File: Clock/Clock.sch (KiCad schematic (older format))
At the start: 39 parts, among them J1 Conn_01x16, J2 Conn_01x16, SW1 SW_Push, SW2 SW_Push, SW3 SW_Push, SW4 SW_Push, U1 74LS76, U2 74LS76, U3 74LS08, U4 74LS08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

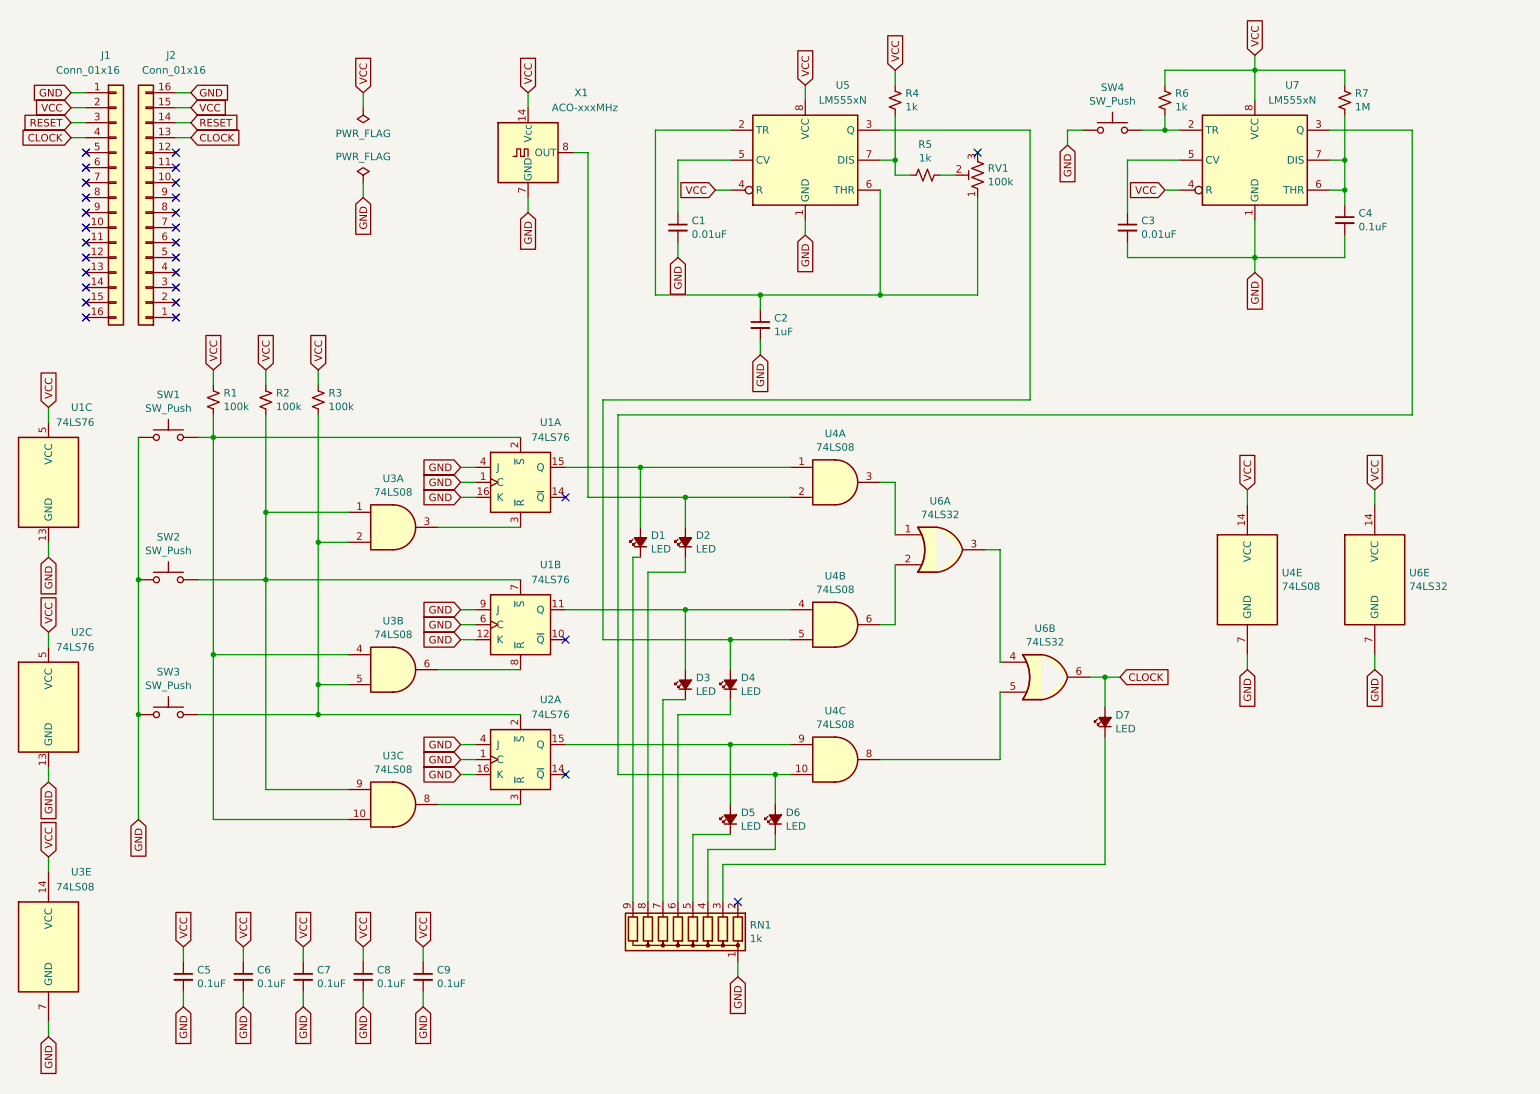
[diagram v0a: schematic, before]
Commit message: Fixed floating inputs; improved power; added parts list; replaced JK latches
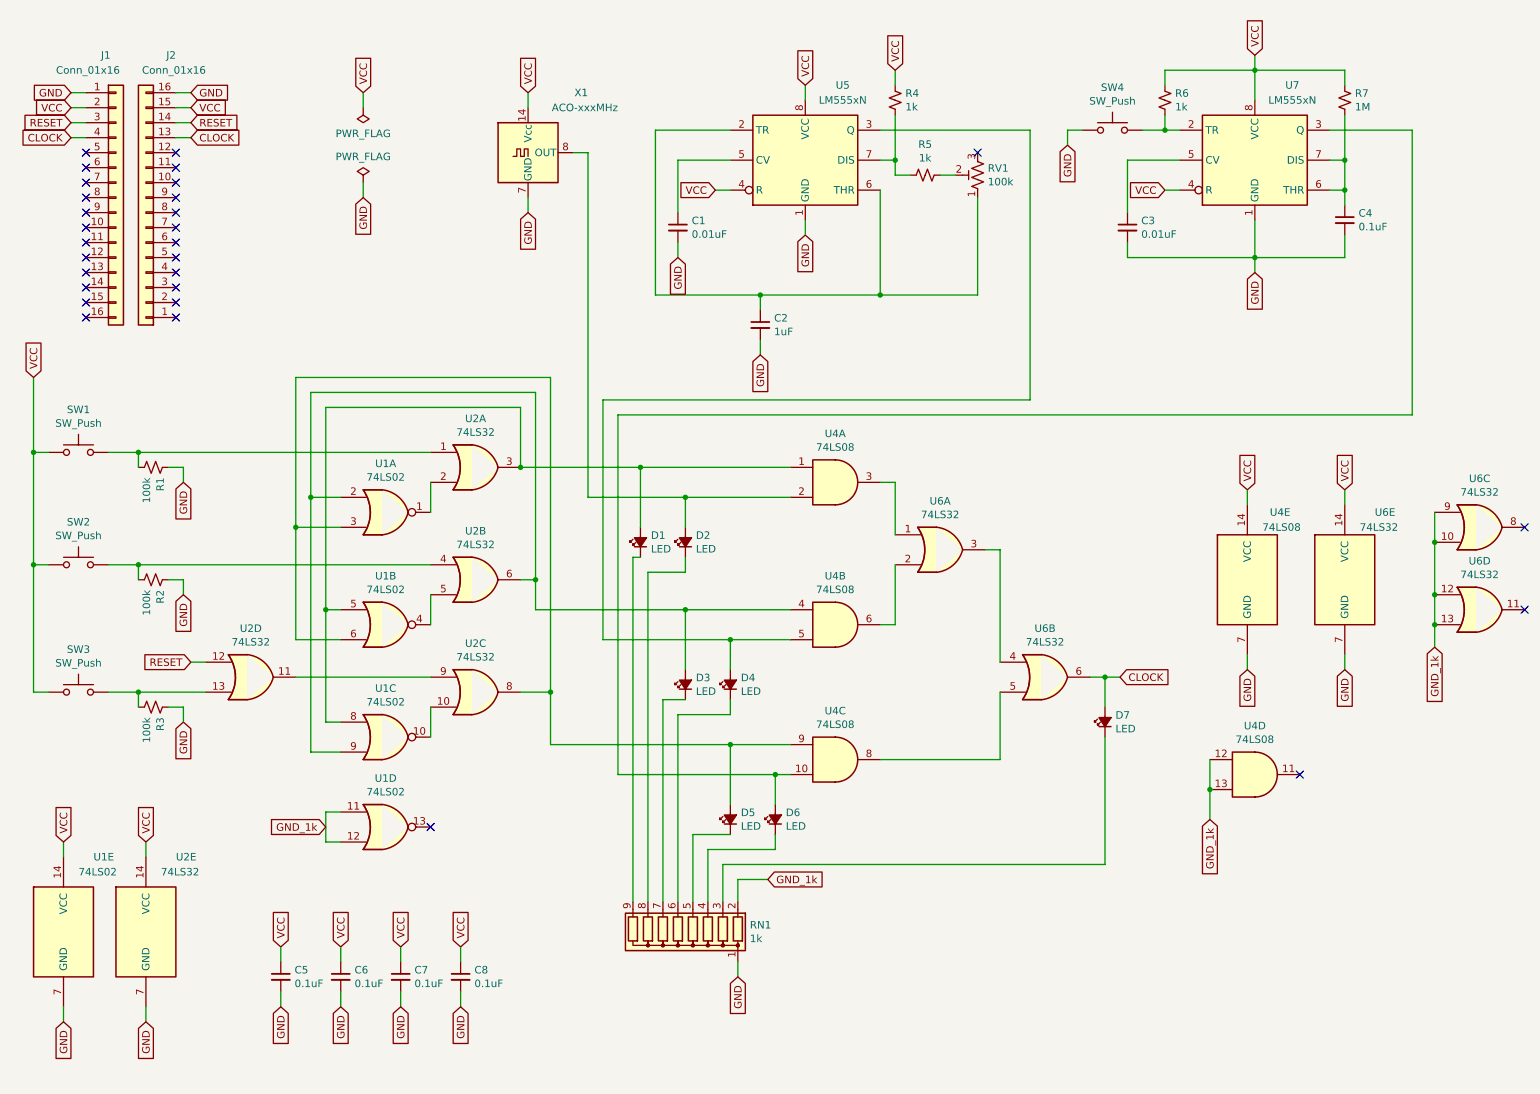
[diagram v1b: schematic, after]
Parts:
- removed C9: 0.1uF, Capacitor_THT:C_Disc_D4.3mm_W1.9mm_P5.00mm, symbol Device:C_Small
- removed U1, U2: 74LS76, Package_DIP:DIP-16_W7.62mm, symbol 74xx:74LS76
- removed U3: 74LS08, Package_DIP:DIP-14_W7.62mm, symbol 74xx:74LS08
- added U1: 74LS02, Package_DIP:DIP-14_W7.62mm, symbol 74xx:74LS02
- added U2: 74LS32, Package_DIP:DIP-14_W7.62mm, symbol 74xx:74LS32
- added unit 4 of U4
- added unit 3 of U6
- added unit 4 of U6
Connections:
- net GND: now also R1.1, R2.1, R3.1, U1.7 (GND), U2.7 (GND); no longer SW1.1, SW2.1, SW3.1
- net RESET: now also U2.12
- net VCC: now also SW1.1, SW2.1, SW3.1, U1.14 (VCC), U2.14 (VCC); no longer R1.1, R2.1, R3.1
- net at D1.2 (A), U4.1: now also U1.5, U1.8, U2.3
- net at R1.2, SW1.2: now also U2.1
- net at D3.2 (A), U4.4: now also U1.2, U1.9, U2.6
- net at R2.2, SW2.2: now also U2.4
- net at D5.2 (A), U4.9: now also U1.3, U1.6, U2.8
- net at R3.2, SW3.2: now also U2.13
- net GND_1k: now reaches RN1.2 (R1)
- net GND_1k: now also U1.11, U1.12, U4.12, U4.13, U6.10, U6.12, U6.13, U6.9
- new net: U1.1, U2.2
- new net: U1.4, U2.5
- new net: U1.10, U2.10
- new net: U2.11, U2.9
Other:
- moved on the sheet: C5, C6, C7, C8, U6E

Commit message: Update all boards to r3, and update revision log and gitignore
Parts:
- RV1: value 100k -> 1M; footprint Potentiometer_THT:Potentiometer_Alps_RK09Y11_Single_Horizontal -> Potentiometer_THT:Potentiometer_Bourns_PTV09A-1_Single_Vertical
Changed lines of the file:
@@
 P 7100 1600
 F 0 "RV1" H 7032 1554 50  0000 R CNN
-F 1 "100k" H 7032 1645 50  0000 R CNN
-F 2 "Potentiometer_THT:Potentiometer_Alps_RK09Y11_Single_Horizontal" H 7100 1600 50  0001 C CNN
+F 1 "1M" H 7032 1645 50  0000 R CNN
+F 2 "Potentiometer_THT:Potentiometer_Bourns_PTV09A-1_Single_Vertical" H 7100 1600 50  0001 C CNN
 F 3 "~" H 7100 1600 50  0001 C CNN
 	1    7100 1600
